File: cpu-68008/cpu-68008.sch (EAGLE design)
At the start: 64 parts, among them IC1 68008, IC11 NE555, IC2 AS6C4008, IC3 39SF010, IC4 DS1244Y, IC5 XR68C681, Q1 8MHz, Q3 3.6864 MHz

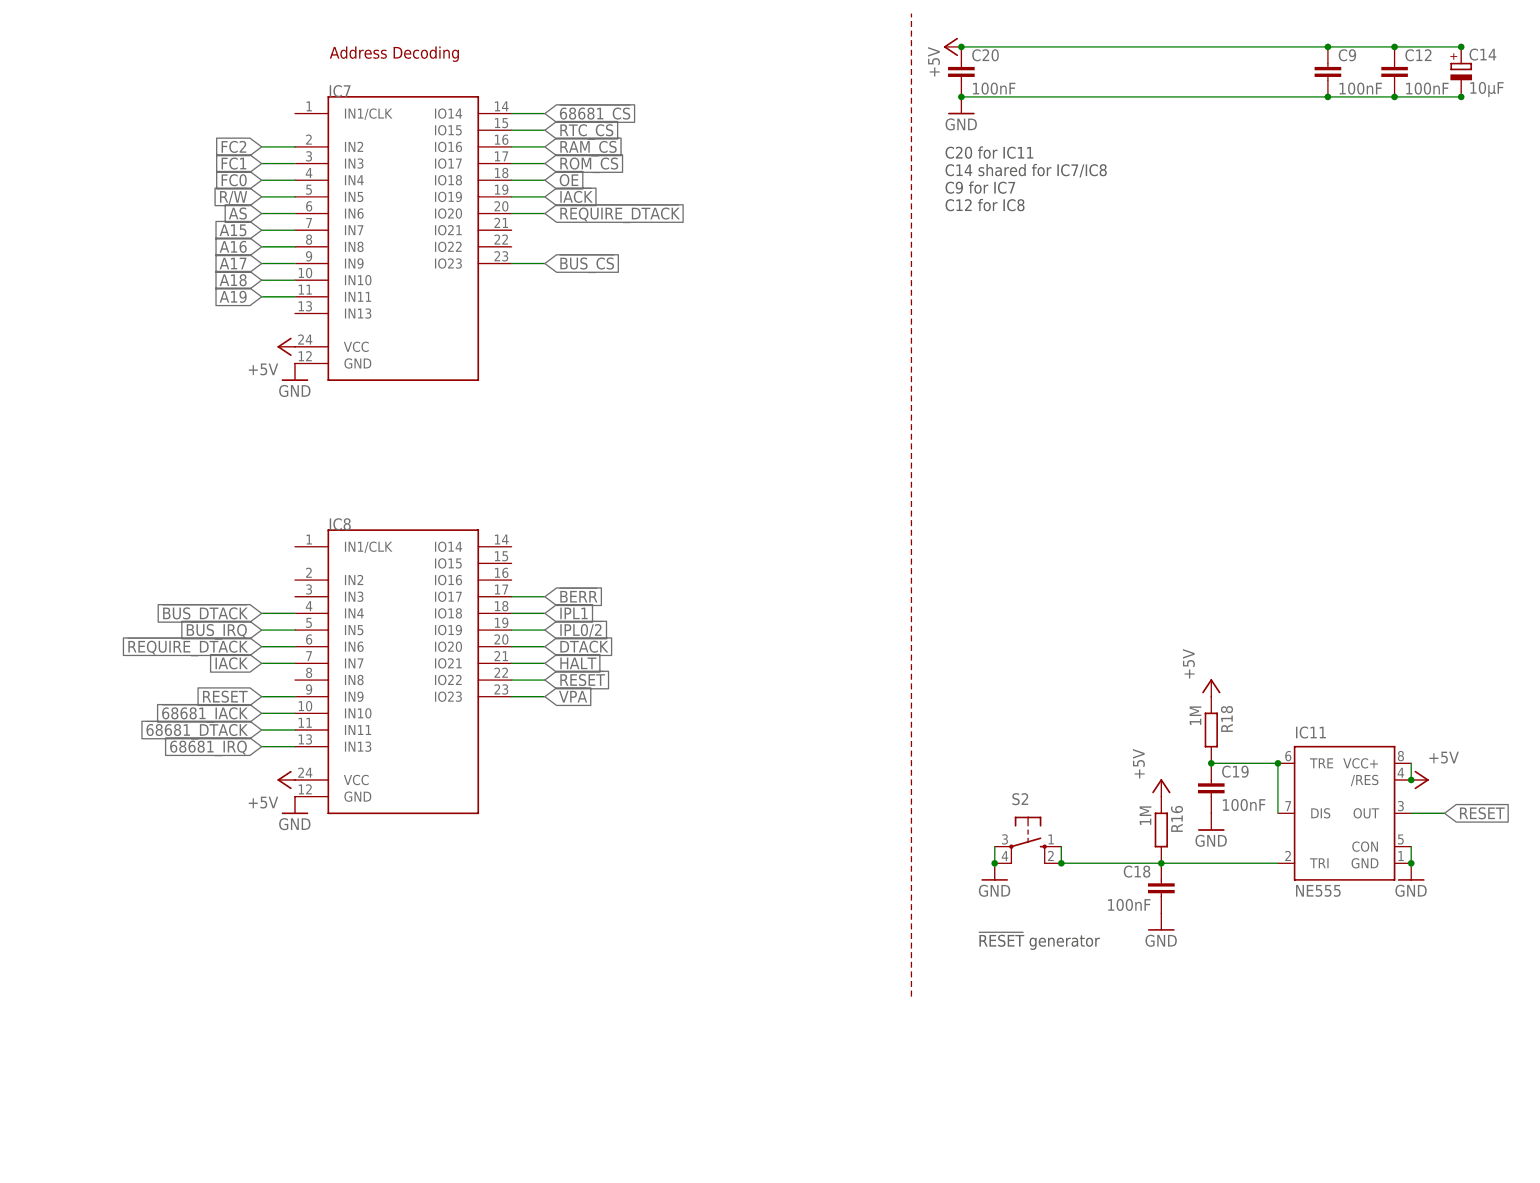
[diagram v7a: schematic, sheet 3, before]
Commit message: added bus error timeout circuit
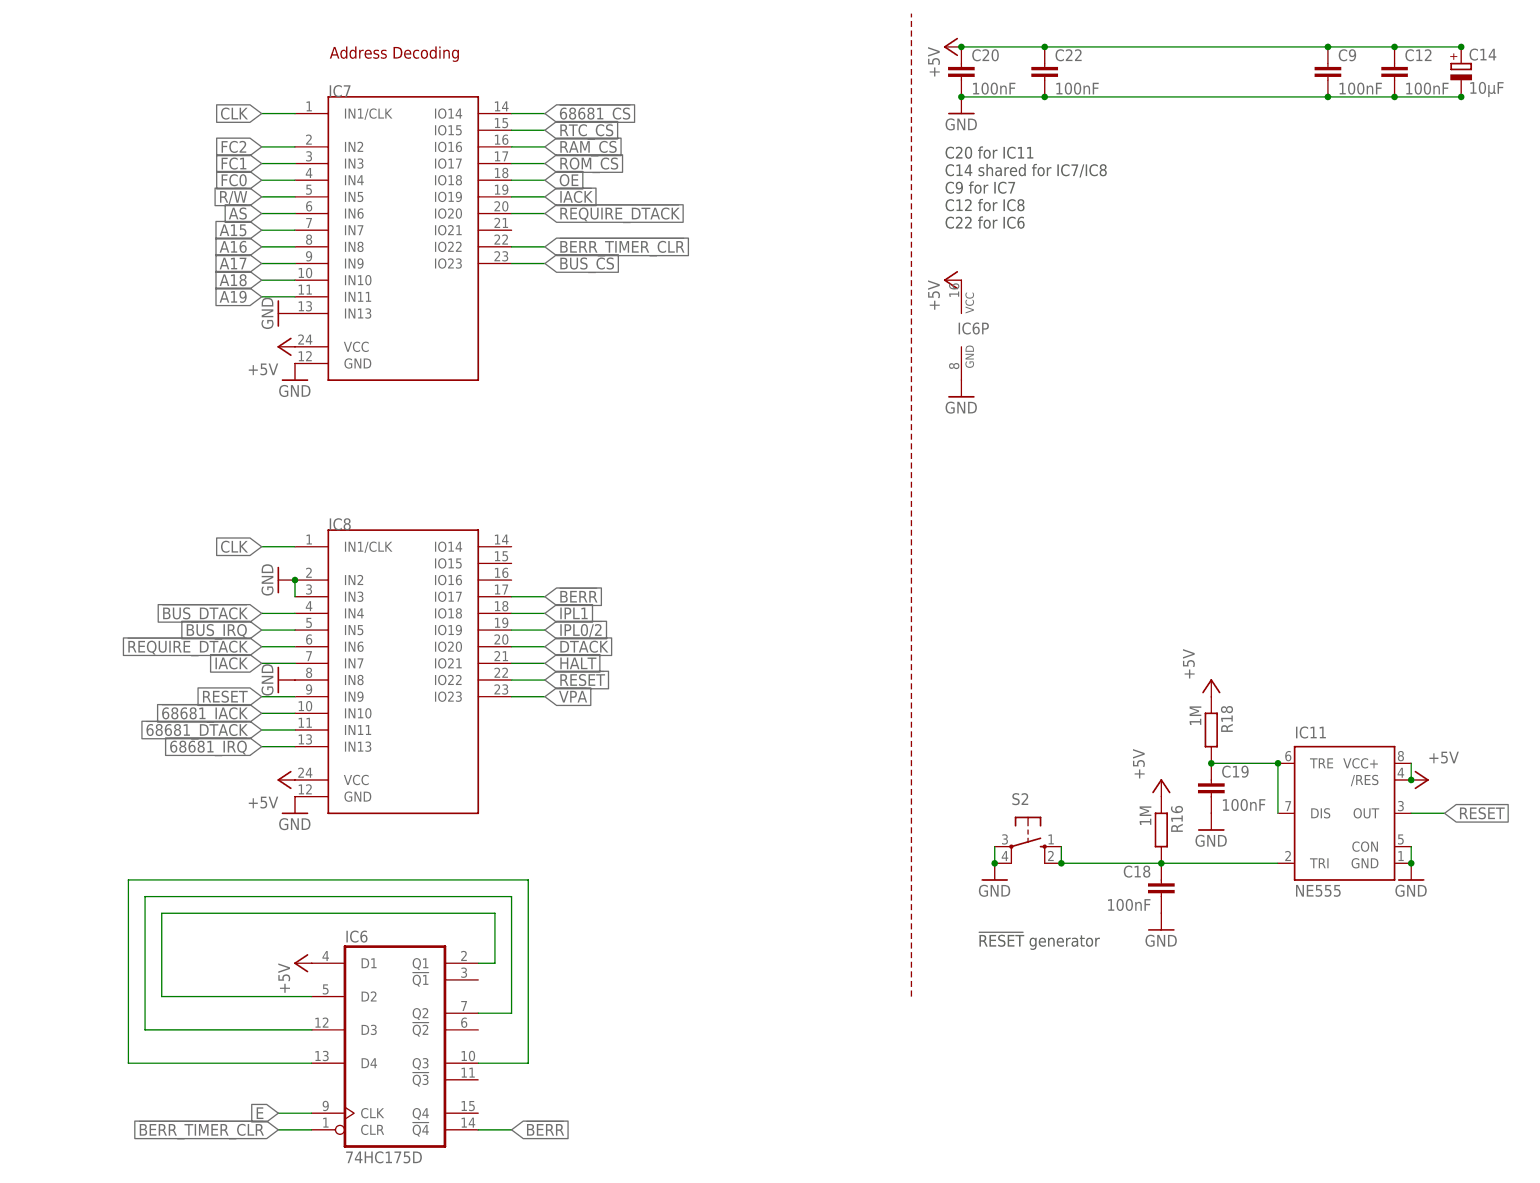
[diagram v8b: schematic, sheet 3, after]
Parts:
- added C22: 100nF, rcl:C-EUC0805
- added IC6: 74HC175D, 74xx-eu:74HC175D
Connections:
- new net !BERR_TIMER_CLR: IC6A.CLR, IC7.IO22
- new net N$5: IC6A.D2, IC6A.Q1
- new net N$6: IC6A.D3, IC6A.Q2
- new net N$8: IC6A.D4, IC6A.Q3
- net !BERR: now also IC6A.!Q4
- net +5V: now also C22.1, IC6A.D1, IC6P.VCC
- net CLK: now also IC7.IN1/CLK, IC8.IN1/CLK
- net E: now also IC6A.CLK
- net GND: now also C22.2, IC6P.GND, IC7.IN13, IC8.IN2, IC8.IN3, IC8.IN8
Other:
- note added: "C20 for IC11 C14 shared for IC7/IC8 C9 for IC7 C12 for IC8 C22 for IC6"
- note removed: "C20 for IC11 C14 shared for IC7/IC8 C9 for IC7 C12 for IC8"
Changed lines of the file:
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@@
 <part name="P+14" library="supply1" library_urn="urn:adsk.eagle:library:371" deviceset="+5V" device=""/>
 <part name="GND34" library="supply1" library_urn="urn:adsk.eagle:library:371" deviceset="GND" device=""/>
+<part name="GND9" library="supply1" library_urn="urn:adsk.eagle:library:371" deviceset="GND" device=""/>
+<part name="GND35" library="supply1" library_urn="urn:adsk.eagle:library:371" deviceset="GND" device=""/>
+<part name="GND36" library="supply1" library_urn="urn:adsk.eagle:library:371" deviceset="GND" device=""/>
+<part name="IC6" library="74xx-eu" library_urn="urn:adsk.eagle:library:85" deviceset="74*175" device="D" package3d_urn="urn:adsk.eagle:package:2010/1" technology="HC"/>
+<part name="P+3" library="supply1" library_urn="urn:adsk.eagle:library:371" deviceset="+5V" device=""/>
+<part name="GND37" library="supply1" library_urn="urn:adsk.eagle:library:371" deviceset="GND" device=""/>
+<part name="C22" library="rcl" library_urn="urn:adsk.eagle:library:334" deviceset="C-EU" device="C0805" package3d_urn="urn:adsk.eagle:package:23617/2" value="100nF">
+<attribute name="MOUSER" value="710-885012207072"/>
+</part>
+<part name="P+20" library="supply1" library_urn="urn:adsk.eagle:library:371" deviceset="+5V" device=""/>
 </parts>
 <sheets>
@@
 C14 shared for IC7/IC8
 C9 for IC7
-C12 for IC8</text>
+C12 for IC8
+C22 for IC6</text>
 <text x="76.2" y="180.34" size="1.778" layer="94" align="top-center">Address Decoding</text>
 </plain>
@@
 <attribute name="VALUE" x="58.42" y="60.96" size="1.778" layer="96"/>
 </instance>
+<instance part="GND9" gate="1" x="58.42" y="99.06" smashed="yes" rot="R270">
+<attribute name="VALUE" x="55.88" y="101.6" size="1.778" layer="96" rot="R270"/>
+</instance>
+<instance part="GND35" gate="1" x="58.42" y="139.7" smashed="yes" rot="R270">
+<attribute name="VALUE" x="55.88" y="142.24" size="1.778" layer="96" rot="R270"/>
+</instance>
+<instance part="GND36" gate="1" x="58.42" y="83.82" smashed="yes" rot="R270">
+<attribute name="VALUE" x="55.88" y="86.36" size="1.778" layer="96" rot="R270"/>
+</instance>
+<instance part="IC6" gate="A" x="76.2" y="27.94" smashed="yes">
+<attribute name="NAME" x="68.58" y="43.815" size="1.778" layer="95"/>
+<attribute name="VALUE" x="68.58" y="10.16" size="1.778" layer="96"/>
+</instance>
+<instance part="IC6" gate="P" x="162.56" y="137.16" smashed="yes">
+<attribute name="NAME" x="161.925" y="136.525" size="1.778" layer="95"/>
+</instance>
+<instance part="P+3" gate="1" x="160.02" y="144.78" smashed="yes" rot="R90">
+<attribute name="VALUE" x="157.48" y="144.78" size="1.778" layer="96" rot="R270"/>
+</instance>
+<instance part="GND37" gate="1" x="162.56" y="127" smashed="yes">
+<attribute name="VALUE" x="160.02" y="124.46" size="1.778" layer="96"/>
+</instance>
+<instance part="C22" gate="G$1" x="175.26" y="177.8" smashed="yes">
+<attribute name="MOUSER" x="175.26" y="177.8" size="1.27" layer="96" align="top-center" display="off"/>
+<attribute name="NAME" x="176.784" y="178.181" size="1.778" layer="95"/>
+<attribute name="VALUE" x="176.784" y="173.101" size="1.778" layer="96"/>
+</instance>
+<instance part="P+20" gate="1" x="60.96" y="40.64" smashed="yes" rot="R90">
+<attribute name="VALUE" x="58.42" y="40.64" size="1.778" layer="96" rot="R270"/>
+</instance>
 </instances>
 <busses>
@@
 <pinref part="P+15" gate="1" pin="+5V"/>
 <pinref part="C20" gate="G$1" pin="1"/>
-<wire x1="162.56" y1="180.34" x2="218.44" y2="180.34" width="0.1524" layer="91"/>
+<wire x1="162.56" y1="180.34" x2="175.26" y2="180.34" width="0.1524" layer="91"/>
 <junction x="162.56" y="180.34"/>
 <pinref part="C9" gate="G$1" pin="1"/>
+<wire x1="175.26" y1="180.34" x2="218.44" y2="180.34" width="0.1524" layer="91"/>
 <wire x1="218.44" y1="180.34" x2="228.6" y2="180.34" width="0.1524" layer="91"/>
 <junction x="218.44" y="180.34"/>
@@
 <wire x1="228.6" y1="180.34" x2="238.76" y2="180.34" width="0.1524" layer="91"/>
 <junction x="228.6" y="180.34"/>
+<pinref part="C22" gate="G$1" pin="1"/>
+<junction x="175.26" y="180.34"/>
 </segment>
 <segment>
@@
 <pinref part="IC8" gate="G$1" pin="VCC"/>
 <pinref part="P+14" gate="1" pin="+5V"/>
+</segment>
+<segment>
+<pinref part="IC6" gate="P" pin="VCC"/>
+<pinref part="P+3" gate="1" pin="+5V"/>
+</segment>
+<segment>
+<pinref part="IC6" gate="A" pin="D1"/>
+<pinref part="P+20" gate="1" pin="+5V"/>
 </segment>
 </net>
@@
 <pinref part="C12" gate="G$1" pin="2"/>
 <junction x="228.6" y="172.72"/>
-<wire x1="218.44" y1="172.72" x2="162.56" y2="172.72" width="0.1524" layer="91"/>
+<wire x1="218.44" y1="172.72" x2="175.26" y2="172.72" width="0.1524" layer="91"/>
+<pinref part="C22" gate="G$1" pin="2"/>
+<wire x1="175.26" y1="172.72" x2="162.56" y2="172.72" width="0.1524" layer="91"/>
+<junction x="175.26" y="172.72"/>
 </segment>
 <segment>
@@
 <pinref part="IC8" gate="G$1" pin="GND"/>
 <pinref part="GND34" gate="1" pin="GND"/>
+</segment>
+<segment>
+<pinref part="IC8" gate="G$1" pin="IN3"/>
+<pinref part="IC8" gate="G$1" pin="IN2"/>
+<wire x1="60.96" y1="96.52" x2="60.96" y2="99.06" width="0.1524" layer="91"/>
+<pinref part="GND9" gate="1" pin="GND"/>
+<junction x="60.96" y="99.06"/>
+</segment>
+<segment>
+<pinref part="IC7" gate="G$1" pin="IN13"/>
+<pinref part="GND35" gate="1" pin="GND"/>
+</segment>
+<segment>
+<pinref part="IC8" gate="G$1" pin="IN8"/>
+<pinref part="GND36" gate="1" pin="GND"/>
+</segment>
+<segment>
+<pinref part="IC6" gate="P" pin="GND"/>
+<pinref part="GND37" gate="1" pin="GND"/>
 </segment>
 </net>
@@
 <label x="99.06" y="96.52" size="1.778" layer="95" xref="yes"/>
 </segment>
+<segment>
+<pinref part="IC6" gate="A" pin="!Q4"/>
+<wire x1="88.9" y1="15.24" x2="93.98" y2="15.24" width="0.1524" layer="91"/>
+<label x="93.98" y="15.24" size="1.778" layer="95" xref="yes"/>
+</segment>
 </net>
 <net name="!68681_CS" class="0">
@@
 </segment>
 </net>
+<net name="CLK" class="0">
+<segment>
+<pinref part="IC8" gate="G$1" pin="IN1/CLK"/>
+<wire x1="60.96" y1="104.14" x2="55.88" y2="104.14" width="0.1524" layer="91"/>
+<label x="55.88" y="104.14" size="1.778" layer="95" rot="R180" xref="yes"/>
+</segment>
+<segment>
+<pinref part="IC7" gate="G$1" pin="IN1/CLK"/>
+<wire x1="60.96" y1="170.18" x2="55.88" y2="170.18" width="0.1524" layer="91"/>
+<label x="55.88" y="170.18" size="1.778" layer="95" rot="R180" xref="yes"/>
+</segment>
+</net>
+<net name="!BERR_TIMER_CLR" class="0">
+<segment>
+<pinref part="IC6" gate="A" pin="CLR"/>
+<wire x1="63.5" y1="15.24" x2="58.42" y2="15.24" width="0.1524" layer="91"/>
+<label x="58.42" y="15.24" size="1.778" layer="95" rot="R180" xref="yes"/>
+</segment>
+<segment>
+<pinref part="IC7" gate="G$1" pin="IO22"/>
+<wire x1="93.98" y1="149.86" x2="99.06" y2="149.86" width="0.1524" layer="91"/>
+<label x="99.06" y="149.86" size="1.778" layer="95" xref="yes"/>
+</segment>
+</net>
+<net name="E" class="0">
+<segment>
+<pinref part="IC6" gate="A" pin="CLK"/>
+<wire x1="63.5" y1="17.78" x2="58.42" y2="17.78" width="0.1524" layer="91"/>
+<label x="58.42" y="17.78" size="1.778" layer="95" rot="R180" xref="yes"/>
+</segment>
+</net>
+<net name="N$5" class="0">
+<segment>
+<pinref part="IC6" gate="A" pin="Q1"/>
+<wire x1="88.9" y1="40.64" x2="91.44" y2="40.64" width="0.1524" layer="91"/>
+<wire x1="91.44" y1="40.64" x2="91.44" y2="48.26" width="0.1524" layer="91"/>
+<wire x1="91.44" y1="48.26" x2="40.64" y2="48.26" width="0.1524" layer="91"/>
+<wire x1="40.64" y1="48.26" x2="40.64" y2="35.56" width="0.1524" layer="91"/>
+<pinref part="IC6" gate="A" pin="D2"/>
+<wire x1="40.64" y1="35.56" x2="63.5" y2="35.56" width="0.1524" layer="91"/>
+</segment>
+</net>
+<net name="N$6" class="0">
+<segment>
+<pinref part="IC6" gate="A" pin="Q2"/>
+<wire x1="88.9" y1="33.02" x2="93.98" y2="33.02" width="0.1524" layer="91"/>
+<wire x1="93.98" y1="33.02" x2="93.98" y2="50.8" width="0.1524" layer="91"/>
+<wire x1="93.98" y1="50.8" x2="38.1" y2="50.8" width="0.1524" layer="91"/>
+<wire x1="38.1" y1="50.8" x2="38.1" y2="30.48" width="0.1524" layer="91"/>
+<pinref part="IC6" gate="A" pin="D3"/>
+<wire x1="38.1" y1="30.48" x2="63.5" y2="30.48" width="0.1524" layer="91"/>
+</segment>
+</net>
+<net name="N$8" class="0">
+<segment>
+<pinref part="IC6" gate="A" pin="Q3"/>
+<wire x1="88.9" y1="25.4" x2="96.52" y2="25.4" width="0.1524" layer="91"/>
+<wire x1="96.52" y1="25.4" x2="96.52" y2="53.34" width="0.1524" layer="91"/>
+<wire x1="96.52" y1="53.34" x2="35.56" y2="53.34" width="0.1524" layer="91"/>
+<wire x1="35.56" y1="53.34" x2="35.56" y2="25.4" width="0.1524" layer="91"/>
+<pinref part="IC6" gate="A" pin="D4"/>
+<wire x1="35.56" y1="25.4" x2="63.5" y2="25.4" width="0.1524" layer="91"/>
+</segment>
+</net>
